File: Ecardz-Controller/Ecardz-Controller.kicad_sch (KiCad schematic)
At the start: 8 parts

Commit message: controller updates
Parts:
- H1: renamed from H5; Part Number (none) -> -
- H2: renamed from H1; Part Number (none) -> -
- H3: renamed from H6; Part Number (none) -> -
- H4: renamed from H2; Part Number (none) -> -
- H5: renamed from H7; Part Number (none) -> -
- H6: renamed from H3; Part Number (none) -> -
- H7: renamed from H8; Part Number (none) -> -
- H8: renamed from H4; Part Number (none) -> -
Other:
- sheet INTERFACE ports: added PWR_INDICATOR; removed none
- sheet MCU ports: added PWR_INDICATOR; removed none
- sheet NFC ports: added PWR; removed none
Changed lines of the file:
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@@
+	(wire
+		(pts
+			(xy 50.8 30.48) (xy 50.8 33.02)
+		)
+		(stroke
+			(width 0)
+			(type default)
+		)
+	)
 	(wire
 		(pts
@@
 	(wire
 		(pts
+			(xy 58.42 33.02) (xy 50.8 33.02)
+		)
+		(stroke
+			(width 0)
+			(type default)
+		)
+	)
+	(wire
+		(pts
 			(xy 25.4 177.8) (xy 25.4 181.61)
 		)
@@
 		(pts
 			(xy 76.2 177.8) (xy 76.2 181.61)
+		)
+		(stroke
+			(width 0)
+			(type default)
+		)
+	)
+	(wire
+		(pts
+			(xy 146.05 101.6) (xy 160.02 101.6)
 		)
 		(stroke
@@
 		(dnp no)
 		(fields_autoplaced yes)
-		(property "Reference" "H8"
+		(property "Reference" "H7"
 			(at 104.14 158.7499 0)
 			(effects
@@
 			)
 		)
-		(property "Datasheet" "~"
+		(property "Datasheet" ""
 			(at 101.6 161.29 0)
 			(effects
@@
 		)
 		(property "Description" "Mounting Hole with connection"
+			(at 101.6 161.29 0)
+			(effects
+				(font
+					(size 1.27 1.27)
+				)
+				(hide yes)
+			)
+		)
+		(property "Part Number" "-"
 			(at 101.6 161.29 0)
 			(effects
@@
 			(project "Ecardz-Controller"
 				(path "/74270717-a116-451e-ac88-5a07ab66056e"
-					(reference "H8")
+					(reference "H7")
 					(unit 1)
 				)
@@
 		(dnp no)
 		(fields_autoplaced yes)
-		(property "Reference" "H5"
+		(property "Reference" "H1"
 			(at 27.94 158.7499 0)
 			(effects
@@
 			)
 		)
-		(property "Datasheet" "~"
+		(property "Datasheet" ""
 			(at 25.4 161.29 0)
 			(effects
@@
 		)
 		(property "Description" "Mounting Hole with connection"
+			(at 25.4 161.29 0)
+			(effects
+				(font
+					(size 1.27 1.27)
+				)
+				(hide yes)
+			)
+		)
+		(property "Part Number" "-"
 			(at 25.4 161.29 0)
 			(effects
@@
 			(project "Ecardz-Controller"
 				(path "/74270717-a116-451e-ac88-5a07ab66056e"
-					(reference "H5")
+					(reference "H1")
 					(unit 1)
 				)
@@
 		(dnp no)
 		(fields_autoplaced yes)
-		(property "Reference" "H2"
+		(property "Reference" "H4"
 			(at 53.34 172.7199 0)
 			(effects
@@
 			)
 		)
-		(property "Datasheet" "~"
+		(property "Datasheet" ""
 			(at 50.8 175.26 0)
 			(effects
@@
 		)
 		(property "Description" "Mounting Hole with connection"
+			(at 50.8 175.26 0)
+			(effects
+				(font
+					(size 1.27 1.27)
+				)
+				(hide yes)
+			)
+		)
+		(property "Part Number" "-"
 			(at 50.8 175.26 0)
 			(effects
@@
 			(project "Ecardz-Controller"
 				(path "/74270717-a116-451e-ac88-5a07ab66056e"
-					(reference "H2")
+					(reference "H4")
 					(unit 1)
 				)
@@
 		(dnp no)
 		(fields_autoplaced yes)
-		(property "Reference" "#PWR05"
+		(property "Reference" "#PWR01"
 			(at 31.75 173.99 0)
 			(effects
@@
 			(project "Ecardz-Controller"
 				(path "/74270717-a116-451e-ac88-5a07ab66056e"
-					(reference "#PWR05")
+					(reference "#PWR01")
 					(unit 1)
 				)
@@
 		(dnp no)
 		(fields_autoplaced yes)
-		(property "Reference" "H3"
+		(property "Reference" "H6"
 			(at 78.74 172.7199 0)
 			(effects
@@
 			)
 		)
-		(property "Datasheet" "~"
+		(property "Datasheet" ""
 			(at 76.2 175.26 0)
 			(effects
@@
 		)
 		(property "Description" "Mounting Hole with connection"
+			(at 76.2 175.26 0)
+			(effects
+				(font
+					(size 1.27 1.27)
+				)
+				(hide yes)
+			)
+		)
+		(property "Part Number" "-"
 			(at 76.2 175.26 0)
 			(effects
@@
 			(project "Ecardz-Controller"
 				(path "/74270717-a116-451e-ac88-5a07ab66056e"
-					(reference "H3")
+					(reference "H6")
 					(unit 1)
 				)
@@
 		(dnp no)
 		(fields_autoplaced yes)
-		(property "Reference" "#PWR01"
+		(property "Reference" "#PWR02"
 			(at 31.75 187.96 0)
 			(effects
@@
 			(project "Ecardz-Controller"
 				(path "/74270717-a116-451e-ac88-5a07ab66056e"
-					(reference "#PWR01")
+					(reference "#PWR02")
 					(unit 1)
 				)
@@
 		(dnp no)
 		(fields_autoplaced yes)
-		(property "Reference" "H4"
+		(property "Reference" "H8"
 			(at 104.14 172.7199 0)
 			(effects
@@
 			)
 		)
-		(property "Datasheet" "~"
+		(property "Datasheet" ""
 			(at 101.6 175.26 0)
 			(effects
@@
 		)
 		(property "Description" "Mounting Hole with connection"
+			(at 101.6 175.26 0)
+			(effects
+				(font
+					(size 1.27 1.27)
+				)
+				(hide yes)
+			)
+		)
+		(property "Part Number" "-"
 			(at 101.6 175.26 0)
 			(effects
@@
 			(project "Ecardz-Controller"
 				(path "/74270717-a116-451e-ac88-5a07ab66056e"
-					(reference "H4")
+					(reference "H8")
 					(unit 1)
 				)
@@
 		(dnp no)
 		(fields_autoplaced yes)
-		(property "Reference" "H1"
+		(property "Reference" "H2"
 			(at 27.94 172.7199 0)
 			(effects
@@
 			)
 		)
-		(property "Datasheet" "~"
+		(property "Datasheet" ""
 			(at 25.4 175.26 0)
 			(effects
@@
 		)
 		(property "Description" "Mounting Hole with connection"
+			(at 25.4 175.26 0)
+			(effects
+				(font
+					(size 1.27 1.27)
+				)
+				(hide yes)
+			)
+		)
+		(property "Part Number" "-"
 			(at 25.4 175.26 0)
 			(effects
@@
 			(project "Ecardz-Controller"
 				(path "/74270717-a116-451e-ac88-5a07ab66056e"
-					(reference "H1")
+					(reference "H2")
 					(unit 1)
 				)
@@
 		(dnp no)
 		(fields_autoplaced yes)
-		(property "Reference" "H6"
+		(property "Reference" "H3"
 			(at 53.34 158.7499 0)
 			(effects
@@
 			)
 		)
-		(property "Datasheet" "~"
+		(property "Datasheet" ""
 			(at 50.8 161.29 0)
 			(effects
@@
 		)
 		(property "Description" "Mounting Hole with connection"
+			(at 50.8 161.29 0)
+			(effects
+				(font
+					(size 1.27 1.27)
+				)
+				(hide yes)
+			)
+		)
+		(property "Part Number" "-"
 			(at 50.8 161.29 0)
 			(effects
@@
 			(project "Ecardz-Controller"
 				(path "/74270717-a116-451e-ac88-5a07ab66056e"
-					(reference "H6")
+					(reference "H3")
+					(unit 1)
+				)
+			)
+		)
+	)
+	(symbol
+		(lib_id "power:+3V3")
+		(at 50.8 30.48 0)
+		(unit 1)
+		(exclude_from_sim no)
+		(in_bom yes)
+		(on_board yes)
+		(dnp no)
+		(fields_autoplaced yes)
+		(property "Reference" "#PWR03"
+			(at 50.8 34.29 0)
+			(effects
+				(font
+					(size 1.27 1.27)
+				)
+				(hide yes)
+			)
+		)
+		(property "Value" "+3V3"
+			(at 50.8 25.4 0)
+			(effects
+				(font
+					(size 1.27 1.27)
+				)
+			)
+		)
+		(property "Footprint" ""
+			(at 50.8 30.48 0)
+			(effects
+				(font
+					(size 1.27 1.27)
+				)
+				(hide yes)
+			)
+		)
+		(property "Datasheet" ""
+			(at 50.8 30.48 0)
+			(effects
+				(font
+					(size 1.27 1.27)
+				)
+				(hide yes)
+			)
+		)
+		(property "Description" "Power symbol creates a global label with name \"+3V3\""
+			(at 50.8 30.48 0)
+			(effects
+				(font
+					(size 1.27 1.27)
+				)
+				(hide yes)
+			)
+		)
+		(pin "1"
+		)
+		(instances
+			(project "Ecardz-Controller"
+				(path "/74270717-a116-451e-ac88-5a07ab66056e"
+					(reference "#PWR03")
 					(unit 1)
 				)
@@
 		(dnp no)
 		(fields_autoplaced yes)
-		(property "Reference" "H7"
+		(property "Reference" "H5"
 			(at 78.74 158.7499 0)
 			(effects
@@
 			)
 		)
-		(property "Datasheet" "~"
+		(property "Datasheet" ""
 			(at 76.2 161.29 0)
 			(effects
@@
 		)
 		(property "Description" "Mounting Hole with connection"
+			(at 76.2 161.29 0)
+			(effects
+				(font
+					(size 1.27 1.27)
+				)
+				(hide yes)
+			)
+		)
+		(property "Part Number" "-"
 			(at 76.2 161.29 0)
 			(effects
@@
 			(project "Ecardz-Controller"
 				(path "/74270717-a116-451e-ac88-5a07ab66056e"
-					(reference "H7")
+					(reference "H5")
 					(unit 1)
 				)
@@
 	(sheet
 		(at 104.14 24.13)
-		(size 41.91 78.74)
+		(size 41.91 81.28)
 		(fields_autoplaced yes)
 		(stroke
@@
 		)
 		(property "Sheetfile" "MCU.kicad_sch"
-			(at 104.14 103.4546 0)
+			(at 104.14 105.9946 0)
 			(effects
 				(font
@@
 		(pin "BUTTON5" output
 			(at 146.05 93.98 0)
+			(effects
+				(font
+					(size 1.27 1.27)
+				)
+				(justify right)
+			)
+		)
+		(pin "PWR_INDICATOR" output
+			(at 146.05 101.6 0)
 			(effects
 				(font
@@
 			)
 		)
+		(pin "PWR" input
+			(at 58.42 33.02 180)
+			(effects
+				(font
+					(size 1.27 1.27)
+				)
+				(justify left)
+			)
+		)
 		(instances
 			(project "Ecardz-Controller"
@@
 	(sheet
 		(at 160.02 24.13)
-		(size 30.48 78.74)
+		(size 30.48 81.28)
 		(fields_autoplaced yes)
 		(stroke
@@
 		)
 		(property "Sheetfile" "INTERFACE.kicad_sch"
-			(at 160.02 103.4546 0)
+			(at 160.02 105.9946 0)
 			(effects
 				(font
@@
 			(effects
 				(font
+					(size 1.27 1.27)
+				)
+				(justify left)
+			)
+		)
+		(pin "PWR_INDICATOR" input
+			(at 160.02 101.6 180)
+			(effects
+				(font

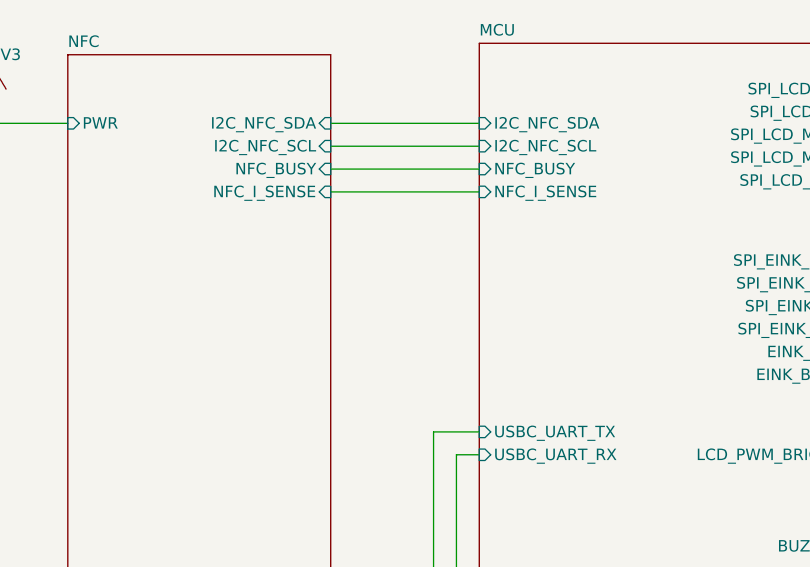
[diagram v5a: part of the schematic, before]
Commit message: updates based on review
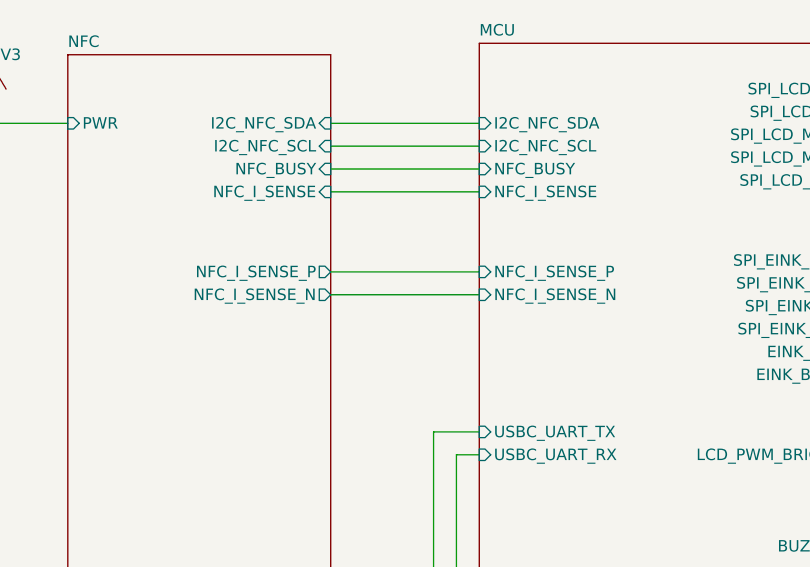
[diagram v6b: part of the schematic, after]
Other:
- sheet MCU ports: added NFC_I_SENSE_N, NFC_I_SENSE_P; removed none
- sheet NFC ports: added NFC_I_SENSE_N, NFC_I_SENSE_P; removed none
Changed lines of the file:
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@@
+	(wire
+		(pts
+			(xy 87.63 52.07) (xy 104.14 52.07)
+		)
+		(stroke
+			(width 0)
+			(type default)
+		)
+	)
 	(wire
 		(pts
@@
 		(pts
 			(xy 146.05 99.06) (xy 160.02 99.06)
+		)
+		(stroke
+			(width 0)
+			(type default)
+		)
+	)
+	(wire
+		(pts
+			(xy 87.63 49.53) (xy 104.14 49.53)
 		)
 		(stroke
@@
 			)
 		)
+		(pin "NFC_I_SENSE_N" input
+			(at 104.14 52.07 180)
+			(effects
+				(font
+					(size 1.27 1.27)
+				)
+				(justify left)
+			)
+		)
+		(pin "NFC_I_SENSE_P" input
+			(at 104.14 49.53 180)
+			(effects
+				(font
+					(size 1.27 1.27)
+				)
+				(justify left)
+			)
+		)
 		(instances
 			(project "Ecardz-Controller"
@@
 			)
 		)
+		(pin "NFC_I_SENSE_P" output
+			(at 87.63 49.53 0)
+			(effects
+				(font
+					(size 1.27 1.27)
+				)
+				(justify right)
+			)
+		)
+		(pin "NFC_I_SENSE_N" output
+			(at 87.63 52.07 0)
+			(effects
+				(font
+					(size 1.27 1.27)
+				)
+				(justify right)
+			)
+		)

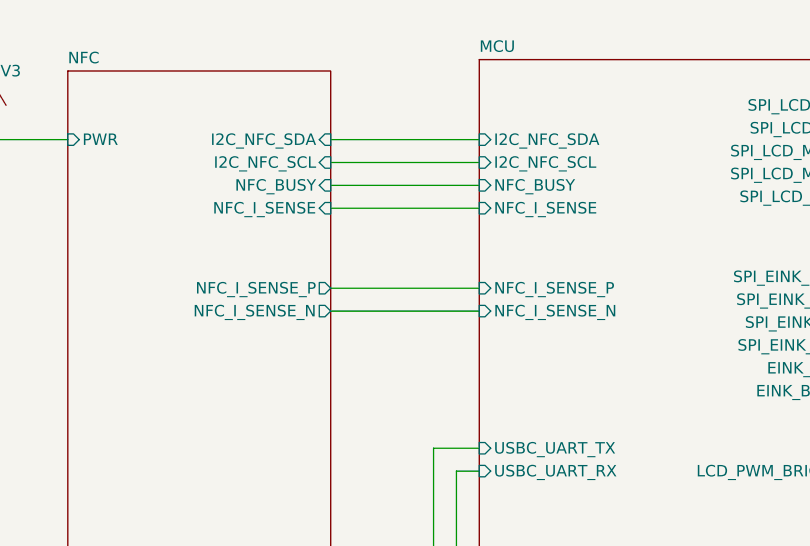
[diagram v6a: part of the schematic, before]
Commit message: added current sense resistor and modified buzzer circuit
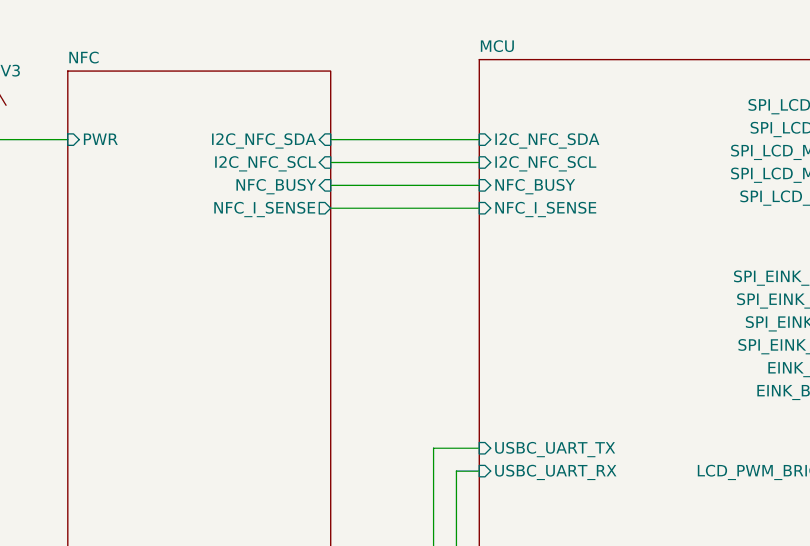
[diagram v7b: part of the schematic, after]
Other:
- sheet MCU ports: added none; removed NFC_I_SENSE_N, NFC_I_SENSE_P
- sheet NFC ports: added none; removed NFC_I_SENSE_N, NFC_I_SENSE_P
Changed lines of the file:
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@@
-	(wire
-		(pts
-			(xy 87.63 52.07) (xy 104.14 52.07)
-		)
-		(stroke
-			(width 0)
-			(type default)
-		)
-	)
 	(wire
 		(pts
@@
 		(pts
 			(xy 146.05 99.06) (xy 160.02 99.06)
-		)
-		(stroke
-			(width 0)
-			(type default)
-		)
-	)
-	(wire
-		(pts
-			(xy 87.63 49.53) (xy 104.14 49.53)
 		)
 		(stroke
@@
 			)
 		)
-		(pin "NFC_I_SENSE_N" input
-			(at 104.14 52.07 180)
-			(effects
-				(font
-					(size 1.27 1.27)
-				)
-				(justify left)
-			)
-		)
-		(pin "NFC_I_SENSE_P" input
-			(at 104.14 49.53 180)
-			(effects
-				(font
-					(size 1.27 1.27)
-				)
-				(justify left)
-			)
-		)
 		(instances
 			(project "Ecardz-Controller"
@@
 			)
 		)
-		(pin "NFC_I_SENSE" input
-			(at 87.63 40.64 0)
-			(effects
-				(font
-					(size 1.27 1.27)
-				)
-				(justify right)
-			)
-		)
 		(pin "PWR" input
 			(at 58.42 33.02 180)
@@
 			)
 		)
-		(pin "NFC_I_SENSE_P" output
-			(at 87.63 49.53 0)
-			(effects
-				(font
-					(size 1.27 1.27)
-				)
-				(justify right)
-			)
-		)
-		(pin "NFC_I_SENSE_N" output
-			(at 87.63 52.07 0)
-			(effects
-				(font
+		(pin "NFC_I_SENSE" output
+			(at 87.63 40.64 0)
+			(effects
+				(font

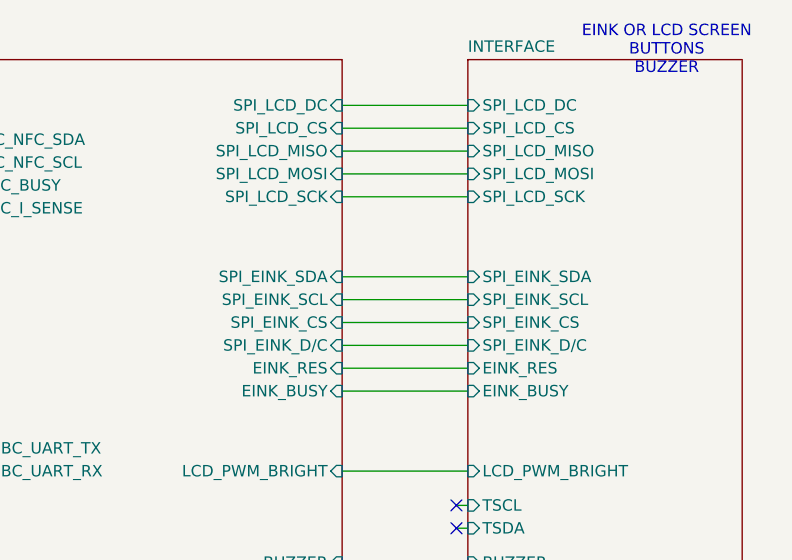
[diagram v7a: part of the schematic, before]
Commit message: redid MCU connections from IOC file from FW team
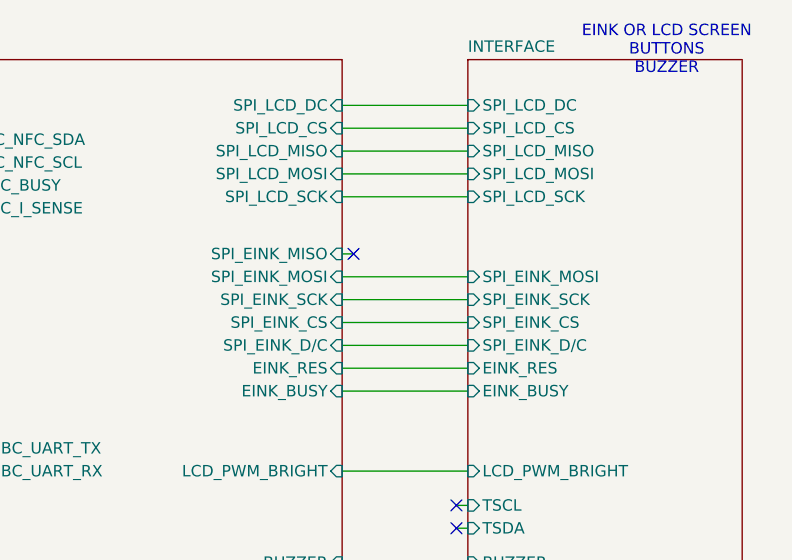
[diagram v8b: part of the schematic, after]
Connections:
- no-connect marks 2 -> 3
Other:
- sheet INTERFACE ports: added SPI_EINK_MOSI, SPI_EINK_SCK; removed SPI_EINK_SCL, SPI_EINK_SDA
- sheet MCU ports: added SPI_EINK_MISO, SPI_EINK_MOSI, SPI_EINK_SCK; removed SPI_EINK_SCL, SPI_EINK_SDA
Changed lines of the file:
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@@
+	)
+	(no_connect
+		(at 147.32 45.72)
 	)
 	(no_connect
@@
 		(pts
 			(xy 101.6 69.85) (xy 104.14 69.85)
+		)
+		(stroke
+			(width 0)
+			(type default)
+		)
+	)
+	(wire
+		(pts
+			(xy 146.05 45.72) (xy 147.32 45.72)
 		)
 		(stroke
@@
 			)
 		)
-		(pin "SPI_EINK_SCL" input
-			(at 146.05 50.8 0)
-			(effects
-				(font
-					(size 1.27 1.27)
-				)
-				(justify right)
-			)
-		)
 		(pin "SPI_EINK_CS" input
 			(at 146.05 53.34 0)
@@
 			)
 		)
-		(pin "SPI_EINK_SDA" input
-			(at 146.05 48.26 0)
-			(effects
-				(font
-					(size 1.27 1.27)
-				)
-				(justify right)
-			)
-		)
 		(pin "EINK_RES" input
 			(at 146.05 58.42 0)
@@
 		(pin "PWR_INDICATOR" output
 			(at 146.05 101.6 0)
+			(effects
+				(font
+					(size 1.27 1.27)
+				)
+				(justify right)
+			)
+		)
+		(pin "SPI_EINK_MOSI" input
+			(at 146.05 48.26 0)
+			(effects
+				(font
+					(size 1.27 1.27)
+				)
+				(justify right)
+			)
+		)
+		(pin "SPI_EINK_MISO" input
+			(at 146.05 45.72 0)
+			(effects
+				(font
+					(size 1.27 1.27)
+				)
+				(justify right)
+			)
+		)
+		(pin "SPI_EINK_SCK" input
+			(at 146.05 50.8 0)
 			(effects
 				(font
@@
 			)
 		)
-		(pin "SPI_EINK_SDA" input
-			(at 160.02 48.26 180)
-			(effects
-				(font
-					(size 1.27 1.27)
-				)
-				(justify left)
-			)
-		)
-		(pin "SPI_EINK_SCL" input
-			(at 160.02 50.8 180)
-			(effects
-				(font
-					(size 1.27 1.27)
-				)
-				(justify left)
-			)
-		)
 		(pin "SPI_EINK_CS" input
 			(at 160.02 53.34 180)
@@
 			(effects
 				(font
+					(size 1.27 1.27)
+				)
+				(justify left)
+			)
+		)
+		(pin "SPI_EINK_MOSI" input
+			(at 160.02 48.26 180)
+			(effects
+				(font
+					(size 1.27 1.27)
+				)
+				(justify left)
+			)
+		)
+		(pin "SPI_EINK_SCK" input
+			(at 160.02 50.8 180)
+			(effects
+				(font
